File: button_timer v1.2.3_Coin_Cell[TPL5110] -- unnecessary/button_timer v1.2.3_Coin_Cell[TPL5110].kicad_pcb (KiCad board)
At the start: 2 copper layers, 21 x 47.8 mm, 27 parts, among them J1 Conn_01x05_Female, Q1 TSM2323, Q2 TSM2323, SW1 SW_Push, SW2 SW_Push, U1 TPS61097A, U2 TPL5110, X1 ESP-12E

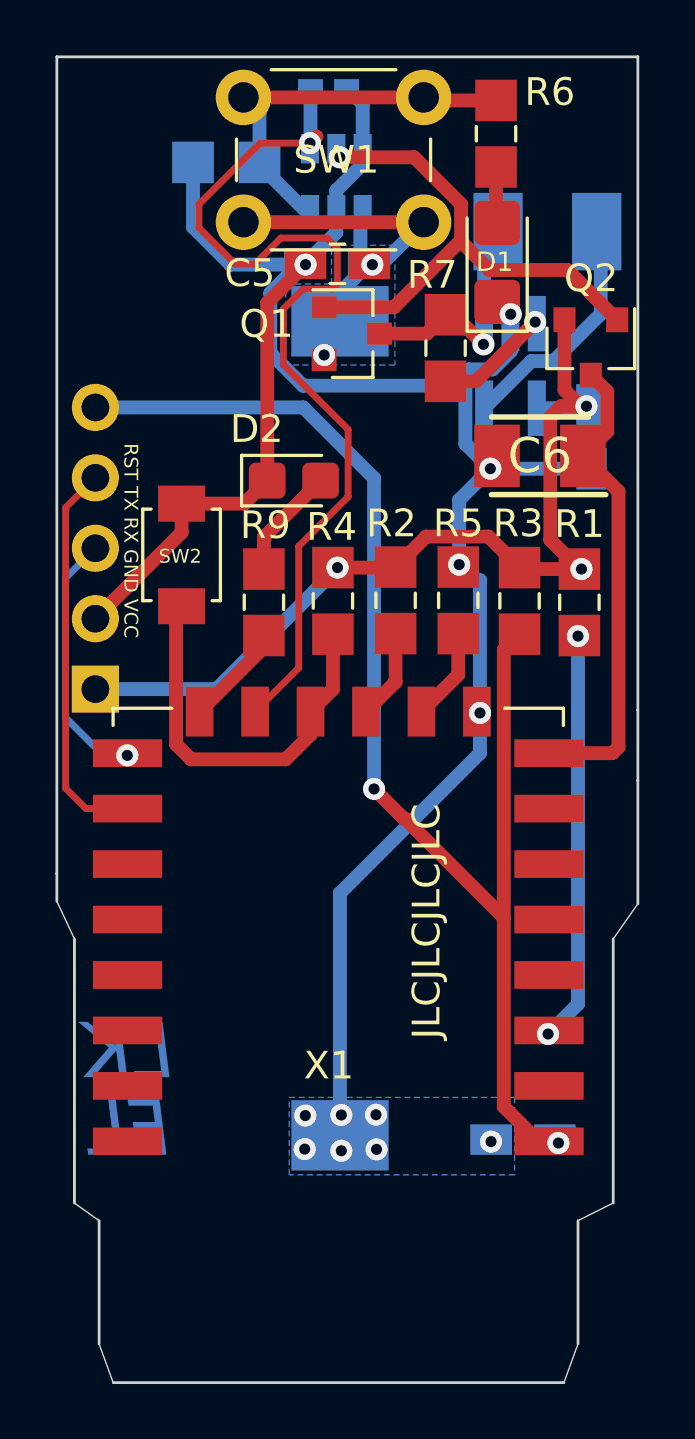
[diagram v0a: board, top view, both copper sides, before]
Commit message: Added 100nF decoupling capacitors between VCC and Ground of the ESP
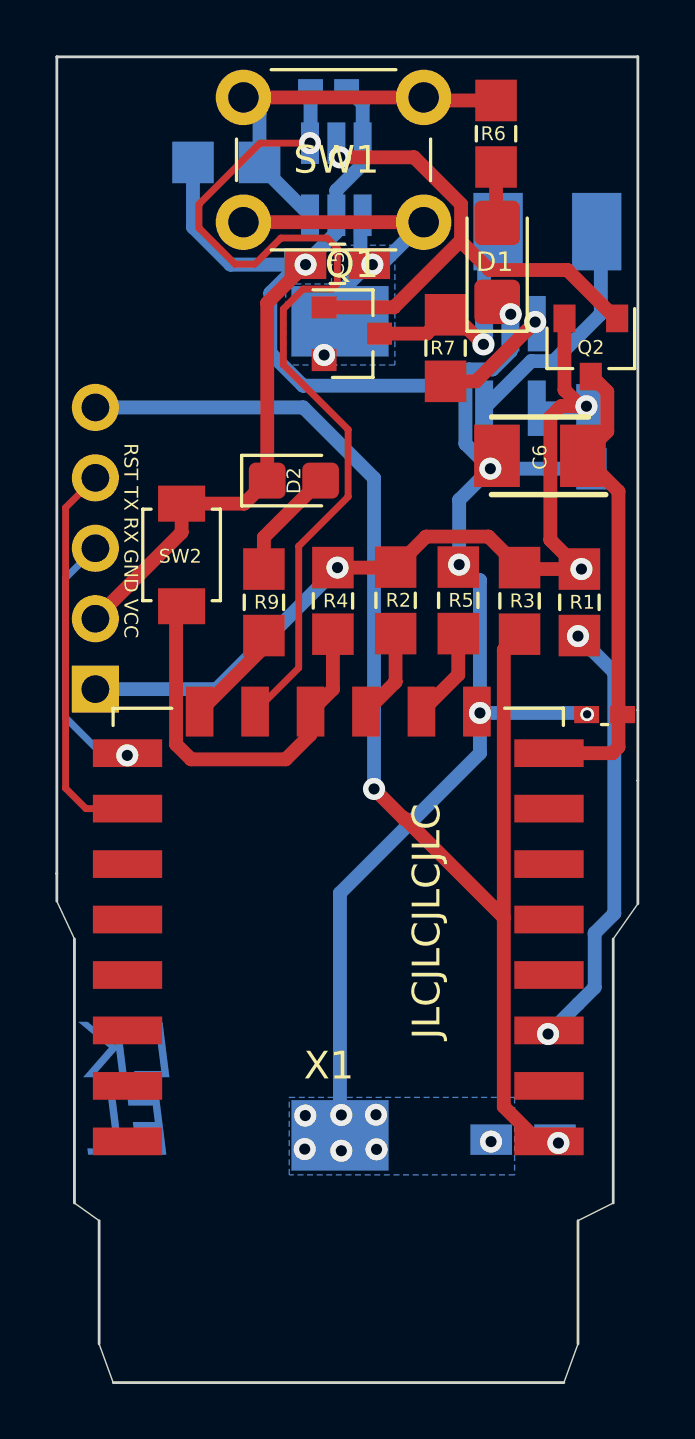
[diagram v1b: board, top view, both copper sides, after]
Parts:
- added C7: 100nF, handsolder:C_0402_1005Metric_Pad0.74x0.62mm_HandSoldermod, F.Cu at (135.3, 78.3)
- D2: footprint LED_SMD:LED_0805_2012Metric_Castellated -> handsolder:LED_0805_2012Metric_Castellated_mod
- Q2: footprint Package_TO_SOT_SMD:SOT-23 -> handsolder:SOT-23
- U2: footprint Package_TO_SOT_SMD:SOT-23-6 -> handsolder:SOT-23-6handsoldering
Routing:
- net /GND: track 80.8 -> 84.7 mm, vias 12 -> 13
- net /EN: track 14.8 -> 15.9 mm
